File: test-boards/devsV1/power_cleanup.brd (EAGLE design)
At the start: 31.7 x 28.9 mm, 18 parts, among them IC2 7805L, IC3 7905L, Q1 BD139, Q2 BD140

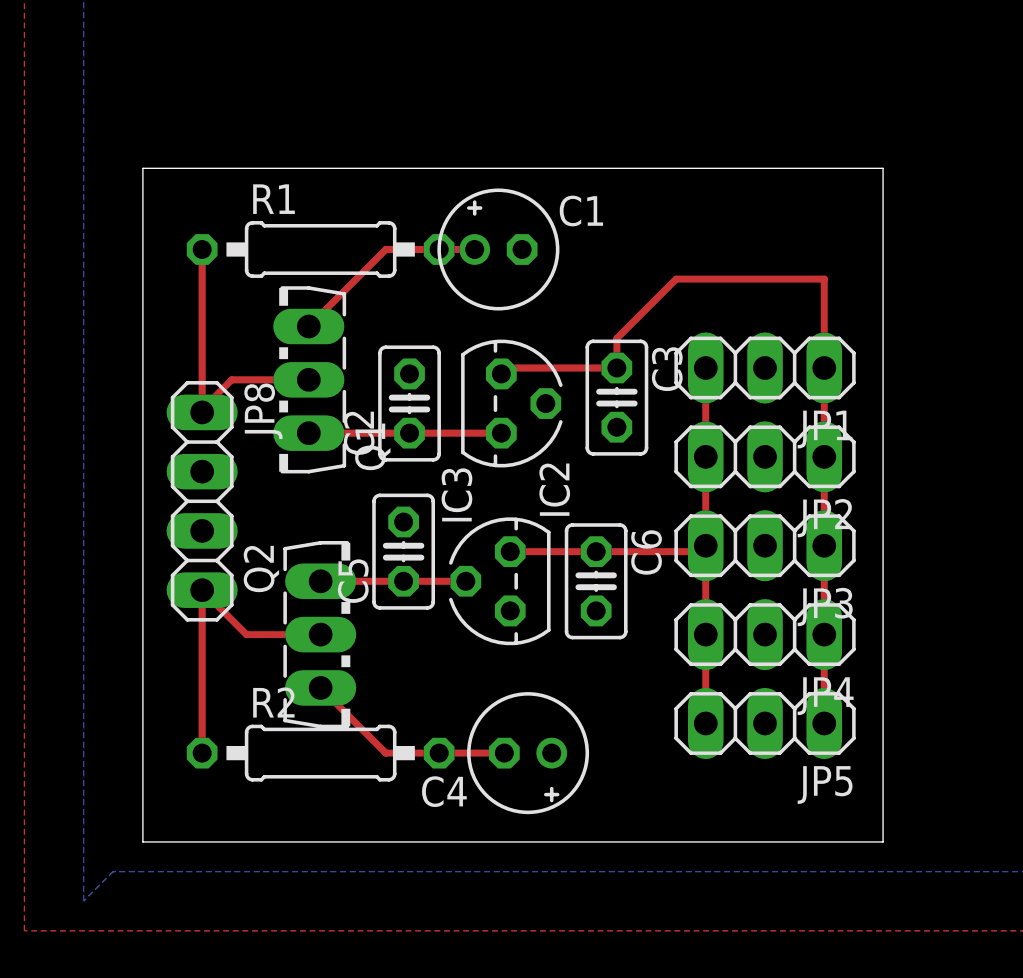
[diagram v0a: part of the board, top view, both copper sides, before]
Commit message: reworked power cleanup for darlington
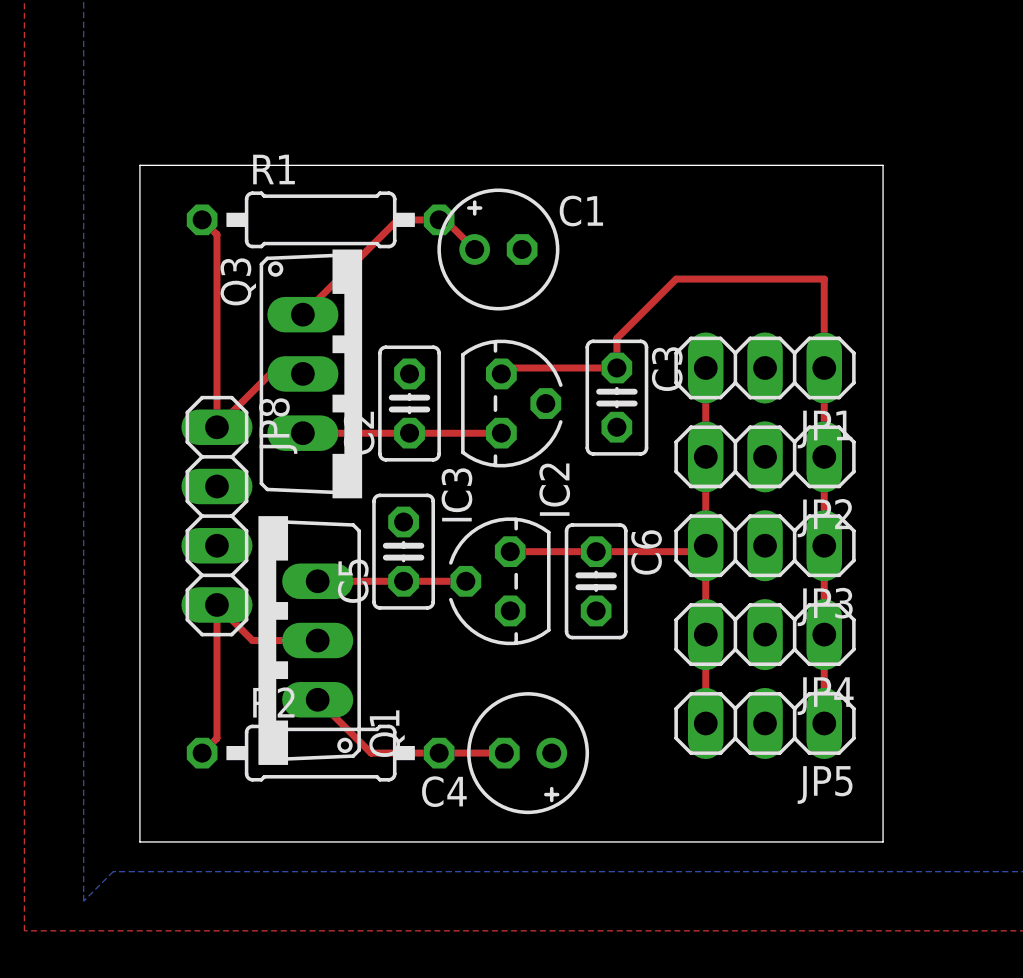
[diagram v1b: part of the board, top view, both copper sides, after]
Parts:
- removed Q2: BD140, transistor-power:TO126AV
- added Q3: MJE3055, transistor-power:TO220AV
- Q1: value BD139 -> MJE2955; device transistor-power:TO126AV -> transistor-power:TO220AV
- moved Q1 11.2 mm to (4.95, 8.64)
- moved R1 1.27 mm to (7.62, 26.7)
- moved JP8 0.90 mm to (3.17, 14.0)
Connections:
- net +12V: now also Q3.C; no longer Q1.C
- net -12V: now also Q1.C; no longer Q2.C
- net N$1: now also Q3.B; no longer Q1.B
- net N$2: now also Q3.E; no longer Q1.E
- net N$4: now also Q1.B; no longer Q2.B
- net N$5: now also Q1.E; no longer Q2.E
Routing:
- net +12V: track 12.2 -> 13.9 mm
- net -12V: track 12.9 -> 11.6 mm
- net N$1: track 8.48 -> 9.58 mm
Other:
- board size 31.7 x 28.9 mm -> 31.9 x 29 mm
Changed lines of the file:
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@@
 <drawing>
 <settings>
-<setting alwaysvectorfont="no"/>
+<setting alwaysvectorfont="yes"/>
 <setting verticaltext="up"/>
 </settings>
-<grid distance="50" unitdist="mil" unit="mil" style="lines" multiple="1" display="no" altdistance="5" altunitdist="mil" altunit="mil"/>
+<grid distance="50" unitdist="mil" unit="mil" style="lines" multiple="1" display="yes" altdistance="5" altunitdist="mil" altunit="mil"/>
 <layers>
 <layer number="1" name="Top" color="4" fill="1" visible="yes" active="yes"/>
@@
 </layers>
 <board>
-<fusionsync huburn="a.cGVyc29uYWw6dWUyOGMwZTIw" projecturn="a.cGVyc29uYWw6dWUyOGMwZTIwIzIwMTgxMjEwMTY0ODcxMzc2" f3durn="urn:adsk.wipprod:dm.lineage:ja7htLZ-SqihchfVz3sSrw" pcbguid="9e3fb264-3e60-492c-8068-f6fe7483c6db" lastpulledtime="" lastsyncedchangeguid="3d090ea0-8f76-008d-368f-4836f7708109"/>
+<fusionsync huburn="a.cGVyc29uYWw6dWUyOGMwZTIw" projecturn="a.cGVyc29uYWw6dWUyOGMwZTIwIzIwMTgxMjEwMTY0ODcxMzc2" f3durn="urn:adsk.wipprod:dm.lineage:ja7htLZ-SqihchfVz3sSrw" pcbguid="9e3fb264-3e60-492c-8068-f6fe7483c6db" lastpulledtime="" lastsyncedchangeguid="308111a5-c2b7-5386-ee46-c01ecf7e6fef"/>
 <plain>
-<wire x1="0" y1="0" x2="31.73" y2="0" width="0" layer="20"/>
-<wire x1="31.73" y1="0" x2="31.73" y2="28.88" width="0" layer="20"/>
-<wire x1="31.73" y1="28.88" x2="0" y2="28.88" width="0" layer="20"/>
-<wire x1="0" y1="28.88" x2="0" y2="0" width="0" layer="20"/>
+<wire x1="-0.127" y1="0" x2="31.73" y2="0" width="0" layer="20"/>
+<wire x1="31.73" y1="0" x2="31.73" y2="29.007" width="0" layer="20"/>
+<wire x1="31.73" y1="29.007" x2="-0.127" y2="29.007" width="0" layer="20"/>
+<wire x1="-0.127" y1="29.007" x2="-0.127" y2="0" width="0" layer="20"/>
 </plain>
 <attributes>
@@
 <attribute name="VALUE" x="17.018" y="14.097" size="1.27" layer="27" ratio="10" rot="R90"/>
 </element>
-<element name="Q1" library="transistor-power" library_urn="urn:adsk.eagle:library:400" package="TO126AV" package3d_urn="urn:adsk.eagle:package:29483/1" value="BD139" x="5.842" y="19.812" smashed="yes" rot="R90">
-<attribute name="NAME" x="10.3886" y="15.8496" size="1.27" layer="25" ratio="10" rot="R90"/>
-<attribute name="VALUE" x="12.1666" y="15.8242" size="1.27" layer="27" ratio="10" rot="R90"/>
-</element>
-<element name="Q2" library="transistor-power" library_urn="urn:adsk.eagle:library:400" package="TO126AV" package3d_urn="urn:adsk.eagle:package:29483/1" value="BD140" x="8.89" y="8.89" smashed="yes" rot="R270">
-<attribute name="NAME" x="4.3434" y="12.8524" size="1.27" layer="25" ratio="10" rot="R270"/>
-<attribute name="VALUE" x="2.5654" y="12.8778" size="1.27" layer="27" ratio="10" rot="R270"/>
-</element>
-<element name="R1" library="rcl" library_urn="urn:adsk.eagle:library:334" package="0207/10" package3d_urn="urn:adsk.eagle:package:23491/2" value="100K" x="7.62" y="25.4" smashed="yes">
-<attribute name="NAME" x="4.572" y="26.924" size="1.27" layer="25" ratio="10"/>
-<attribute name="SPICEPREFIX" value="R" x="26.67" y="-16.51" size="1.778" layer="27" display="off"/>
-<attribute name="VALUE" x="5.3594" y="24.765" size="1.27" layer="27" ratio="10"/>
+<element name="R1" library="rcl" library_urn="urn:adsk.eagle:library:334" package="0207/10" package3d_urn="urn:adsk.eagle:package:23491/2" value="100K" x="7.62" y="26.67" smashed="yes">
+<attribute name="NAME" x="4.572" y="28.194" size="1.27" layer="25" ratio="10"/>
+<attribute name="SPICEPREFIX" value="R" x="26.67" y="-15.24" size="1.778" layer="27" display="off"/>
+<attribute name="VALUE" x="5.3594" y="26.035" size="1.27" layer="27" ratio="10"/>
 </element>
 <element name="R2" library="rcl" library_urn="urn:adsk.eagle:library:334" package="0207/10" package3d_urn="urn:adsk.eagle:package:23491/2" value="100K" x="7.62" y="3.81" smashed="yes">
@@
 <attribute name="VALUE" x="5.3594" y="3.175" size="1.27" layer="27" ratio="10"/>
 </element>
-<element name="JP8" library="pinhead" library_urn="urn:adsk.eagle:library:325" package="1X04" package3d_urn="urn:adsk.eagle:package:22407/2" value="" x="2.54" y="14.605" smashed="yes" rot="R270">
-<attribute name="NAME" x="4.3688" y="19.7612" size="1.27" layer="25" ratio="10" rot="R270"/>
-<attribute name="VALUE" x="-0.635" y="19.685" size="1.27" layer="27" rot="R270"/>
+<element name="JP8" library="pinhead" library_urn="urn:adsk.eagle:library:325" package="1X04" package3d_urn="urn:adsk.eagle:package:22407/2" value="" x="3.175" y="13.97" smashed="yes" rot="R270">
+<attribute name="NAME" x="5.0038" y="19.1262" size="1.27" layer="25" ratio="10" rot="R270"/>
+<attribute name="VALUE" x="0" y="19.05" size="1.27" layer="27" rot="R270"/>
 </element>
 <element name="JP1" library="pinhead" library_urn="urn:adsk.eagle:library:325" package="1X03" package3d_urn="urn:adsk.eagle:package:22458/2" value="" x="26.67" y="20.32" smashed="yes" rot="R180">
@@
 <attribute name="NAME" x="30.5562" y="3.2512" size="1.27" layer="25" ratio="10" rot="R180"/>
 <attribute name="VALUE" x="30.48" y="8.255" size="1.27" layer="27" rot="R180"/>
+</element>
+<element name="Q3" library="transistor-power" library_urn="urn:adsk.eagle:library:400" package="TO220AV" package3d_urn="urn:adsk.eagle:package:29487/2" value="MJE3055" x="9.398" y="20.066" smashed="yes" rot="R270">
+<attribute name="NAME" x="3.3528" y="25.146" size="1.27" layer="25" ratio="10" rot="R270"/>
+<attribute name="VALUE" x="1.778" y="25.146" size="1.27" layer="27" ratio="10" rot="R270"/>
+</element>
+<element name="Q1" library="transistor-power" library_urn="urn:adsk.eagle:library:400" package="TO220AV" package3d_urn="urn:adsk.eagle:package:29487/2" value="MJE2955" x="4.953" y="8.636" smashed="yes" rot="R90">
+<attribute name="NAME" x="10.9982" y="3.556" size="1.27" layer="25" ratio="10" rot="R90"/>
+<attribute name="VALUE" x="12.573" y="3.556" size="1.27" layer="27" ratio="10" rot="R90"/>
 </element>
 </elements>
@@
 <signal name="+12V">
 <contactref element="R1" pad="1"/>
-<contactref element="Q1" pad="C"/>
-<wire x1="7.112" y1="19.812" x2="3.81" y2="19.812" width="0.3" layer="1"/>
 <contactref element="JP8" pad="1"/>
-<wire x1="2.54" y1="18.415" x2="2.54" y2="25.4" width="0.3" layer="1"/>
-<wire x1="3.81" y1="19.812" x2="2.54" y2="18.542" width="0.3" layer="1"/>
-<wire x1="2.54" y1="18.542" x2="2.54" y2="18.415" width="0.3" layer="1"/>
+<wire x1="3.175" y1="26.035" x2="2.54" y2="26.67" width="0.3" layer="1"/>
+<wire x1="3.175" y1="26.035" x2="3.175" y2="17.78" width="0.3" layer="1"/>
+<wire x1="3.175" y1="17.78" x2="3.175" y2="17.907" width="0.3" layer="1"/>
+<contactref element="Q3" pad="C"/>
+<wire x1="3.175" y1="17.78" x2="5.461" y2="20.066" width="0.3" layer="1"/>
+<wire x1="5.461" y1="20.066" x2="6.858" y2="20.066" width="0.3" layer="1"/>
 </signal>
 <signal name="-12V">
 <contactref element="R2" pad="1"/>
-<contactref element="Q2" pad="C"/>
 <contactref element="JP8" pad="4"/>
-<wire x1="2.54" y1="10.795" x2="4.445" y2="8.89" width="0.3" layer="1"/>
-<wire x1="4.445" y1="8.89" x2="7.62" y2="8.89" width="0.3" layer="1"/>
-<wire x1="2.54" y1="3.81" x2="2.54" y2="10.795" width="0.3" layer="1"/>
+<wire x1="3.175" y1="10.16" x2="3.175" y2="4.445" width="0.3" layer="1"/>
+<wire x1="2.54" y1="3.81" x2="3.175" y2="4.445" width="0.3" layer="1"/>
+<contactref element="Q1" pad="C"/>
+<wire x1="7.493" y1="8.636" x2="4.699" y2="8.636" width="0.3" layer="1"/>
+<wire x1="4.699" y1="8.636" x2="3.175" y2="10.16" width="0.3" layer="1"/>
 </signal>
 <signal name="N$1">
 <contactref element="C1" pad="+"/>
-<contactref element="Q1" pad="B"/>
 <contactref element="R1" pad="2"/>
-<wire x1="12.7" y1="25.4" x2="14.224" y2="25.4" width="0.3" layer="1"/>
-<wire x1="12.7" y1="25.4" x2="10.414" y2="25.4" width="0.3" layer="1"/>
-<wire x1="10.414" y1="25.4" x2="7.112" y2="22.098" width="0.3" layer="1"/>
+<wire x1="12.954" y1="26.67" x2="14.224" y2="25.4" width="0.3" layer="1"/>
+<wire x1="12.954" y1="26.67" x2="12.7" y2="26.67" width="0.3" layer="1"/>
+<contactref element="Q3" pad="B"/>
+<wire x1="6.858" y1="22.606" x2="10.922" y2="26.67" width="0.3" layer="1"/>
+<wire x1="10.922" y1="26.67" x2="12.7" y2="26.67" width="0.3" layer="1"/>
 </signal>
 <signal name="N$2">
-<contactref element="Q1" pad="E"/>
 <contactref element="IC2" pad="3"/>
 <contactref element="C2" pad="1"/>
-<wire x1="7.112" y1="17.526" x2="11.43" y2="17.526" width="0.3" layer="1"/>
 <wire x1="11.43" y1="17.526" x2="15.367" y2="17.526" width="0.3" layer="1"/>
+<contactref element="Q3" pad="E"/>
+<wire x1="6.858" y1="17.526" x2="11.43" y2="17.526" width="0.3" layer="1"/>
 </signal>
 <signal name="N$4">
-<contactref element="Q2" pad="B"/>
 <contactref element="C4" pad="-"/>
 <contactref element="R2" pad="2"/>
 <wire x1="12.700003125" y1="3.81" x2="15.493996875" y2="3.81" width="0.3" layer="1"/>
-<wire x1="7.620003125" y1="6.603996875" x2="10.414" y2="3.81" width="0.3" layer="1"/>
-<wire x1="10.414" y1="3.81" x2="12.7" y2="3.81" width="0.3" layer="1"/>
+<contactref element="Q1" pad="B"/>
+<wire x1="12.7" y1="3.81" x2="9.779" y2="3.81" width="0.3" layer="1"/>
+<wire x1="9.779" y1="3.81" x2="7.493" y2="6.096" width="0.3" layer="1"/>
 <wire x1="15.493996875" y1="3.81" x2="15.494" y2="3.81" width="0" layer="19" extent="1-1"/>
 <wire x1="12.7" y1="3.81" x2="12.700003125" y2="3.81" width="0" layer="19" extent="1-1"/>
-<wire x1="7.62" y1="6.604" x2="7.620003125" y2="6.603996875" width="0" layer="19" extent="1-1"/>
 </signal>
 <signal name="N$5">
 <contactref element="C5" pad="1"/>
-<contactref element="Q2" pad="E"/>
 <contactref element="IC3" pad="2"/>
-<wire x1="7.62" y1="11.176" x2="11.176" y2="11.176" width="0.3" layer="1"/>
 <wire x1="11.176" y1="11.176" x2="13.843" y2="11.176" width="0.3" layer="1"/>
+<contactref element="Q1" pad="E"/>
+<wire x1="7.493" y1="11.176" x2="11.176" y2="11.176" width="0.3" layer="1"/>
 </signal>
 </signals>

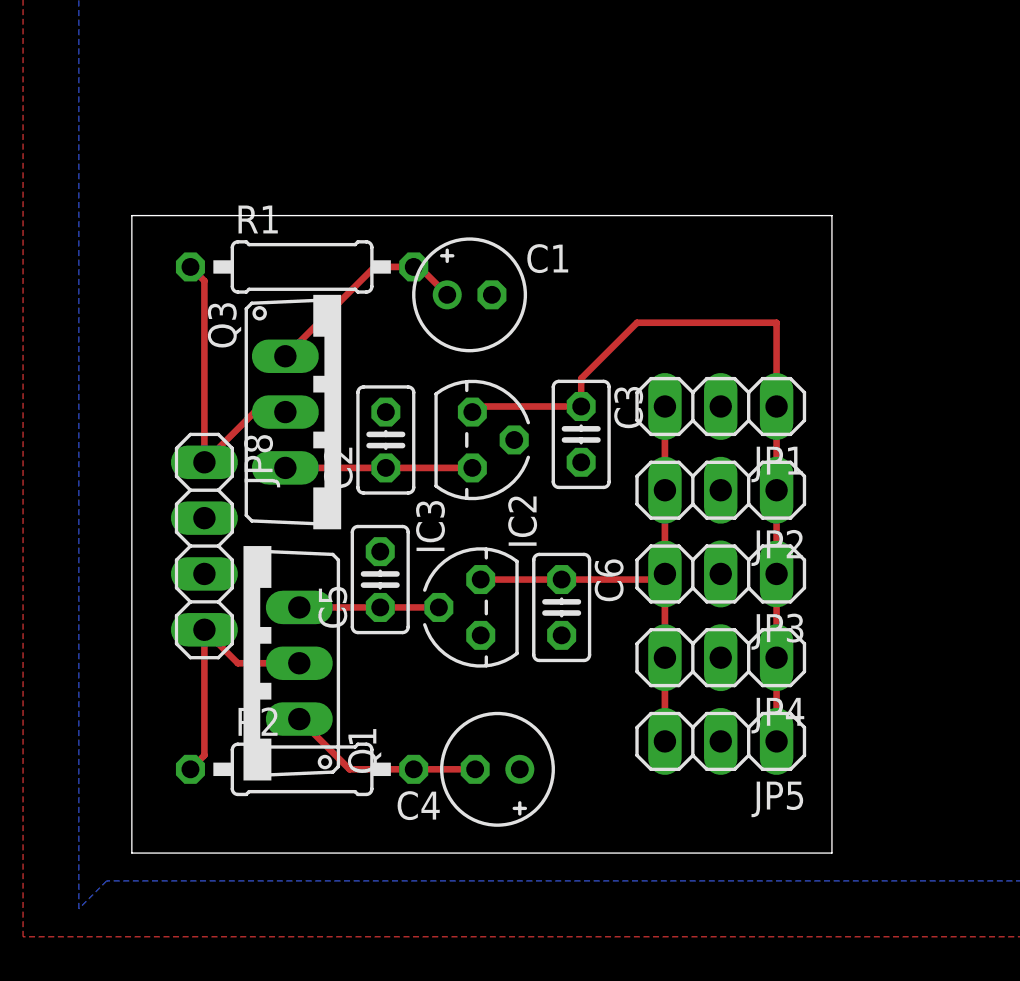
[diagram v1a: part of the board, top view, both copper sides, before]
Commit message: reduced size of some boards
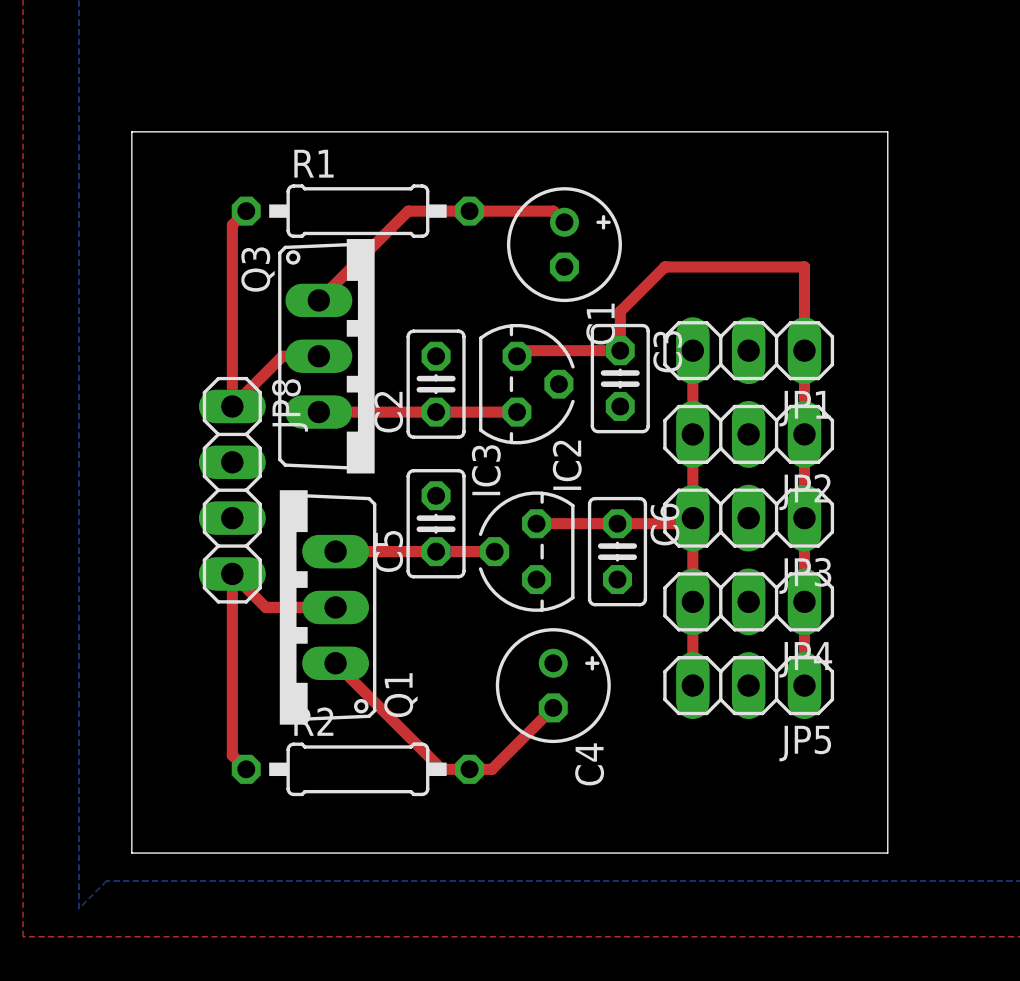
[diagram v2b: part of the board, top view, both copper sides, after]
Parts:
- moved C1 4.89 mm to (19.6, 27.7), turned to 270 degrees
- moved C4 4.58 mm to (19.1, 7.62), turned to 270 degrees
- moved C5 3.59 mm to (13.7, 15.0)
- moved IC3 3.59 mm to (18.3, 13.7)
- moved R1 3.59 mm to (10.2, 29.2)
- moved C6 3.59 mm to (22.0, 13.7)
- moved C2 3.42 mm to (13.7, 21.3)
- moved IC2 3.25 mm to (17.4, 21.3)
- moved C3 3.10 mm to (22.1, 21.6)
- moved Q1 3.03 mm to (6.60, 11.2)
- moved Q3 2.96 mm to (10.9, 22.6)
- moved JP8 2.84 mm to (4.45, 16.5)
- moved JP3 2.84 mm to (27.9, 15.2)
- moved JP5 2.84 mm to (27.9, 7.62)
- moved JP1 2.84 mm to (27.9, 22.9)
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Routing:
- net N$4: track 8.95 -> 13.1 mm
- net N$1: track 9.58 -> 13.1 mm
- net -12V: track 11.6 -> 14.5 mm
- net -5V: track 23.7 -> 22.5 mm
- net N$5: track 6.35 -> 7.24 mm
- net N$2: track 8.51 -> 9.02 mm
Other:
- board size 31.9 x 29 mm -> 34.4 x 32.8 mm

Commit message: measurement device init
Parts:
- moved Q3 1.80 mm to (9.65, 21.3)
- moved JP8 1.80 mm to (3.17, 15.2)
- moved C5 1.80 mm to (12.4, 13.7)
- moved C4 1.80 mm to (17.8, 6.35)
- moved JP5 1.80 mm to (26.7, 6.35)
- moved Q1 1.80 mm to (5.33, 9.91)
- moved R2 1.80 mm to (8.89, 2.54)
- moved C1 1.80 mm to (18.3, 26.4)
- moved C2 1.80 mm to (12.4, 20.1)
- moved C3 1.80 mm to (20.8, 20.3)
- moved C6 1.80 mm to (20.7, 12.4)
- moved IC2 1.80 mm to (16.1, 20.1)
- moved IC3 1.80 mm to (17.0, 12.4)
- moved JP1 1.80 mm to (26.7, 21.6)
- moved JP2 1.80 mm to (26.7, 17.8)
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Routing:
- net N$4: track 13.1 -> 14.6 mm
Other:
- board size 34.4 x 32.8 mm -> 31.9 x 30.3 mm
